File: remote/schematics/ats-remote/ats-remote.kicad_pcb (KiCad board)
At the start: 4 copper layers, 34 x 39 mm, 34 parts, among them J1 PWR, J4 Conn_01x02_Male, U1 RFM95W-915S2

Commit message: update schematic and pcb
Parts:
- removed GPS ANT: GPS_ANT, ats-remote:GPS_ANT_SR4G008
- added AE1: GPS_ANT, ats-remote:GPS_ANT_SR4G008, F.Cu at (140.5, 38.3)
- added C14: 10n, Capacitor_SMD:C_0805_2012Metric_Pad1.18x1.45mm_HandSolder, F.Cu at (140.2, 43.6)
- added L3: 33n, Inductor_SMD:L_0603_1608Metric_Pad1.05x0.95mm_HandSolder, F.Cu at (142.1, 46.9)
- added L4: 33n, Inductor_SMD:L_0603_1608Metric_Pad1.05x0.95mm_HandSolder, F.Cu at (142.1, 43.4)
- AE2: renamed from LORA ANT
- C13, C8: value 2.2u -> 2u2
- C6: value 100p -> 2u2
- C7: value 100p -> 10n
- J3: renamed from SPI; value Conn_01x04_Male -> SPI
- J4: value Conn_01x02_Male -> UART
- R1, R2: value 2.2k -> 2k2
- R5: value 22 -> 2k2
- moved J3 3.90 mm to (114.2, 62.9), turned to 180 degrees
- moved L1 3.06 mm to (140.0, 47.3)
- moved C11 2.77 mm to (142.4, 51.1), turned to 90 degrees
- moved D1 1.20 mm to (141.3, 65.3)
- moved D2 1.20 mm to (141.3, 68.0)
- moved D3 1.20 mm to (141.3, 62.5)
- moved C8 1.00 mm to (140.2, 51.1), turned to 90 degrees
- renumbered ICSP to J2, PIC18 to U2, YIC to U3
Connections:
- J3 pad 1: LORA_SCK -> LORA_NSS
- J3 pad 2: LORA_MOSI -> LORA_MISO
- J3 pad 3: LORA_MISO -> LORA_MOSI
- J3 pad 4: LORA_NSS -> LORA_SCK
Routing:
- net +3V3: track 32.1 -> 109.8 mm
- net Net-(AE1-Pad2): track 0.00 -> 4.19 mm
- net GND: track 69.2 -> 71.3 mm, vias 59 -> 83
- net Net-(C11-Pad2): track 15.4 -> 13.4 mm
- net Net-(D2-Pad2): track 3.76 -> 2.56 mm
- net Net-(D1-Pad2): track 3.76 -> 2.56 mm
- net Net-(D3-Pad2): track 3.76 -> 2.56 mm
- net LORA_NSS: track 45.5 -> 46.5 mm
- net Net-(C14-Pad2): track 10.1 -> 9.14 mm
- added copper zone on 3v3.Cu, net GND
- removed copper zone on 3v3.Cu, net +3V3
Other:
- net class 50ohm @ JLCPCB type JLC7628 added: clearance 0.6, trace_width 0.29337, via_dia 0.5, via_drill 0.3
- rule trace_min: 0.3 -> 0.2

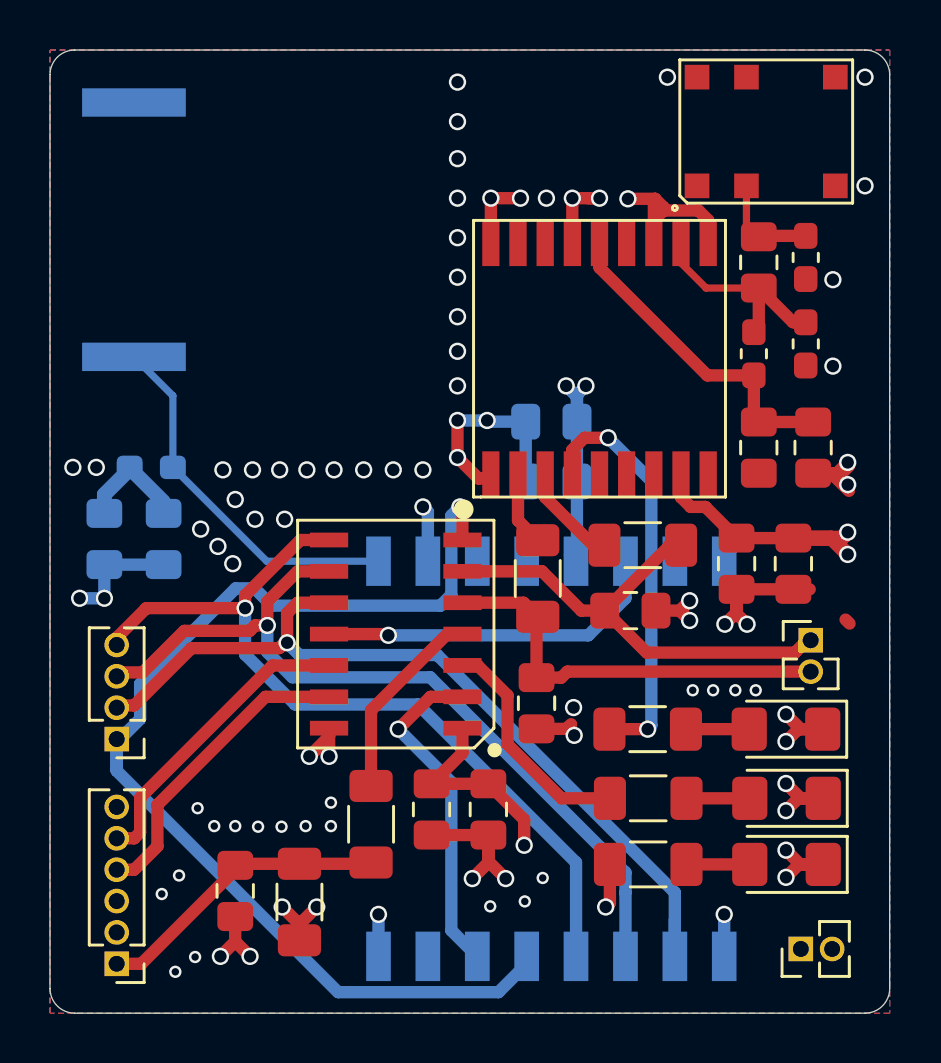
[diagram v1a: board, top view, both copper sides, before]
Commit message: add silk screen
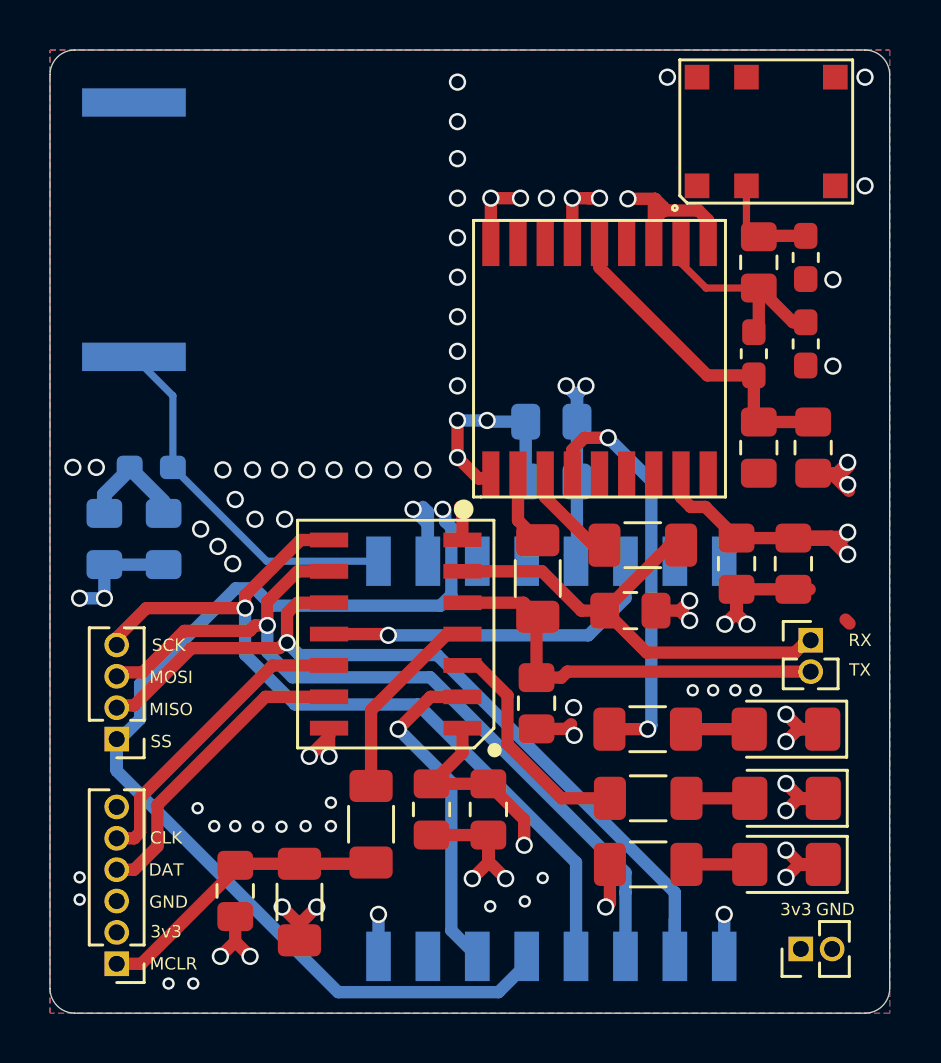
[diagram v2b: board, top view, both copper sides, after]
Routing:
- net GND: track 71.3 -> 73.7 mm
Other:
- board text added: "3v3"
- board text added: "CLK"
- board text added: "DAT"
- board text added: "GND"
- board text added: "MCLR"
- board text added: "MISO"
- board text added: "MOSI"
- board text added: "RX"
- board text added: "SCK"
- board text added: "SS"
- board text added: "TX"
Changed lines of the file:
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@@
   (general
     (thickness 1.6)
-    (drawings 8)
-    (tracks 395)
+    (drawings 21)
+    (tracks 398)
     (zones 0)
     (modules 37)
@@
   )
   (layers
-    (0 F.Cu signal)
-    (1 GND.Cu power)
-    (2 3v3.Cu power)
+    (0 F.Cu signal hide)
+    (1 GND.Cu power hide)
+    (2 3v3.Cu power hide)
     (31 B.Cu signal)
     (32 B.Adhes user)
@@
     (pad 2 smd rect (at -6.425 4.6 270) (size 1.15 4.2) (layers B.Cu B.Paste B.Mask))
   )
+  (gr_text TX (at 144.3 60.1) (layer F.SilkS)
+    (effects (font (size 0.5 0.5) (thickness 0.1)))
+  )
+  (gr_text "RX\n" (at 144.3 58.9) (layer F.SilkS)
+    (effects (font (size 0.5 0.5) (thickness 0.1)))
+  )
+  (gr_text "GND\n" (at 143.3 69.8) (layer F.SilkS)
+    (effects (font (size 0.5 0.5) (thickness 0.1)))
+  )
+  (gr_text "3v3\n" (at 141.7 69.8) (layer F.SilkS)
+    (effects (font (size 0.5 0.5) (thickness 0.1)))
+  )
+  (gr_text CLK (at 116.2 66.9) (layer F.SilkS)
+    (effects (font (size 0.5 0.5) (thickness 0.1)))
+  )
+  (gr_text DAT (at 116.2 68.2) (layer F.SilkS)
+    (effects (font (size 0.5 0.5) (thickness 0.1)))
+  )
+  (gr_text "GND\n" (at 116.3 69.5) (layer F.SilkS)
+    (effects (font (size 0.5 0.5) (thickness 0.1)))
+  )
+  (gr_text "3v3\n" (at 116.2 70.7) (layer F.SilkS)
+    (effects (font (size 0.5 0.5) (thickness 0.1)))
+  )
+  (gr_text MCLR (at 116.5 72) (layer F.SilkS)
+    (effects (font (size 0.5 0.5) (thickness 0.1)))
+  )
+  (gr_text "SCK\n" (at 116.3 59.1) (layer F.SilkS)
+    (effects (font (size 0.5 0.5) (thickness 0.1)))
+  )
+  (gr_text MOSI (at 116.4 60.4) (layer F.SilkS)
+    (effects (font (size 0.5 0.5) (thickness 0.1)))
+  )
+  (gr_text "MISO\n" (at 116.4 61.7) (layer F.SilkS)
+    (effects (font (size 0.5 0.5) (thickness 0.1)))
+  )
+  (gr_text SS (at 116 63) (layer F.SilkS)
+    (effects (font (size 0.5 0.5) (thickness 0.1)))
+  )
   (gr_arc (start 112.5 73) (end 111.5 73) (angle -90) (layer Edge.Cuts) (width 0.05))
   (gr_arc (start 144.5 73) (end 144.5 74) (angle -90) (layer Edge.Cuts) (width 0.05))
@@
   (segment (start 127.750001 64.650001) (end 127.750001 70.650001) (width 0.5) (layer B.Cu) (net 1))
   (segment (start 125.6 62.5) (end 127.750001 64.650001) (width 0.5) (layer B.Cu) (net 1))
-  (via (at 128.1 53.5) (size 0.7) (drill 0.5) (layers F.Cu B.Cu) (net 2))
+  (via (at 127.4 53.6) (size 0.7) (drill 0.5) (layers F.Cu B.Cu) (net 2))
   (segment (start 130.8 71.389998) (end 130.8 71.389998) (width 0.5) (layer B.Cu) (net 2))
   (segment (start 119.015999 56.799999) (end 115.150001 60.665997) (width 0.5) (layer B.Cu) (net 2))
@@
   (segment (start 127.310003 57.499999) (end 120.484001 57.499999) (width 0.5) (layer B.Cu) (net 2))
   (segment (start 127.750001 57.060001) (end 127.310003 57.499999) (width 0.5) (layer B.Cu) (net 2))
-  (segment (start 127.750001 53.849999) (end 127.750001 57.060001) (width 0.5) (layer B.Cu) (net 2))
-  (segment (start 128.1 53.5) (end 127.750001 53.849999) (width 0.5) (layer B.Cu) (net 2))
   (segment (start 114.2 64.184002) (end 114.2 62.81) (width 0.5) (layer B.Cu) (net 2))
   (segment (start 123.165999 73.150001) (end 114.2 64.184002) (width 0.5) (layer B.Cu) (net 2))
@@
   (segment (start 115.150001 62.086001) (end 114.336002 62.9) (width 0.5) (layer B.Cu) (net 2))
   (segment (start 115.150001 60.665997) (end 115.150001 62.086001) (width 0.5) (layer B.Cu) (net 2))
+  (segment (start 127.50001 54.090008) (end 127.50001 53.6) (width 0.5) (layer B.Cu) (net 2))
+  (segment (start 127.750001 54.339999) (end 127.50001 54.090008) (width 0.5) (layer B.Cu) (net 2))
+  (segment (start 127.750001 57.060001) (end 127.750001 54.339999) (width 0.5) (layer B.Cu) (net 2))
   (via (at 119.4 57.6) (size 0.7) (drill 0.5) (layers F.Cu B.Cu) (net 3))
   (segment (start 132.8 72.010002) (end 132.8 72.010002) (width 0.5) (layer B.Cu) (net 3))
@@
   (via (at 125.4 52) (size 0.7) (drill 0.5) (layers F.Cu B.Cu) (net 18))
   (via (at 126.6 52) (size 0.7) (drill 0.5) (layers F.Cu B.Cu) (net 18))
-  (via (at 126.6 53.5) (size 0.7) (drill 0.5) (layers F.Cu B.Cu) (net 18))
+  (via (at 126.2 53.6) (size 0.7) (drill 0.5) (layers F.Cu B.Cu) (net 18))
   (segment (start 126.8 53.7) (end 126.6 53.5) (width 0.5) (layer B.Cu) (net 18))
   (segment (start 126.8 55.7) (end 126.8 53.7) (width 0.5) (layer B.Cu) (net 18))
@@
   (via (at 129.325 69.675) (size 0.5) (drill 0.3) (layers F.Cu B.Cu) (net 18))
   (via (at 131.45 68.525) (size 0.5) (drill 0.3) (layers F.Cu B.Cu) (net 18))
-  (via (at 117.375 71.725) (size 0.5) (drill 0.3) (layers F.Cu B.Cu) (net 18))
-  (via (at 116.575 72.325) (size 0.5) (drill 0.3) (layers F.Cu B.Cu) (net 18))
-  (via (at 116.725 68.425) (size 0.5) (drill 0.3) (layers F.Cu B.Cu) (net 18))
-  (via (at 116.025 69.175) (size 0.5) (drill 0.3) (layers F.Cu B.Cu) (net 18))
+  (via (at 117.3 72.8) (size 0.5) (drill 0.3) (layers F.Cu B.Cu) (net 18))
+  (via (at 116.3 72.8) (size 0.5) (drill 0.3) (layers F.Cu B.Cu) (net 18))
+  (via (at 112.7 68.5) (size 0.5) (drill 0.3) (layers F.Cu B.Cu) (net 18))
+  (via (at 112.7 69.4) (size 0.5) (drill 0.3) (layers F.Cu B.Cu) (net 18))
   (via (at 117.475 65.7) (size 0.5) (drill 0.3) (layers F.Cu B.Cu) (net 18))
   (via (at 118.15 66.425) (size 0.5) (drill 0.3) (layers F.Cu B.Cu) (net 18))
@@
   (segment (start 143.3375 52.1375) (end 143.8 52.6) (width 0.5) (layer F.Cu) (net 18))
   (segment (start 142.4 52.1375) (end 143.3375 52.1375) (width 0.5) (layer F.Cu) (net 18))
+  (segment (start 126.8 54.2) (end 126.2 53.6) (width 0.5) (layer B.Cu) (net 18))
+  (segment (start 126.8 55.7) (end 126.8 54.2) (width 0.5) (layer B.Cu) (net 18))
   (segment (start 121.64 67.91) (end 121.6 67.95) (width 0.5) (layer F.Cu) (net 19))
   (segment (start 119.0625 67.95) (end 119 68.0125) (width 0.5) (layer F.Cu) (net 19))

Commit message: update silk screen
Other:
- board text added: "GPS ANT"
- board text added: "LORA ANT"
- board text added: "PIC18F06"
- board text added: "YIC71009EBGG"
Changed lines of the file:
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@@
   (general
     (thickness 1.6)
-    (drawings 21)
+    (drawings 25)
     (tracks 398)
     (zones 0)
@@
   )
   (layers
-    (0 F.Cu signal hide)
-    (1 GND.Cu power hide)
-    (2 3v3.Cu power hide)
+    (0 F.Cu signal)
+    (1 GND.Cu power)
+    (2 3v3.Cu power)
     (31 B.Cu signal)
     (32 B.Adhes user)
@@
     (pad 2 smd rect (at -6.425 4.6 270) (size 1.15 4.2) (layers B.Cu B.Paste B.Mask))
   )
+  (gr_text "GPS ANT" (at 136.5 39.5 90) (layer F.SilkS)
+    (effects (font (size 0.5 0.5) (thickness 0.1)))
+  )
+  (gr_text "LORA ANT\n" (at 115.2 48.8) (layer B.SilkS)
+    (effects (font (size 0.5 0.5) (thickness 0.1)) (justify mirror))
+  )
+  (gr_text YIC71009EBGG (at 136.2 53.6) (layer F.SilkS)
+    (effects (font (size 0.5 0.5) (thickness 0.1)))
+  )
+  (gr_text PIC18F06 (at 123.2 53.5) (layer F.SilkS)
+    (effects (font (size 0.5 0.5) (thickness 0.1)))
+  )
   (gr_text TX (at 144.3 60.1) (layer F.SilkS)

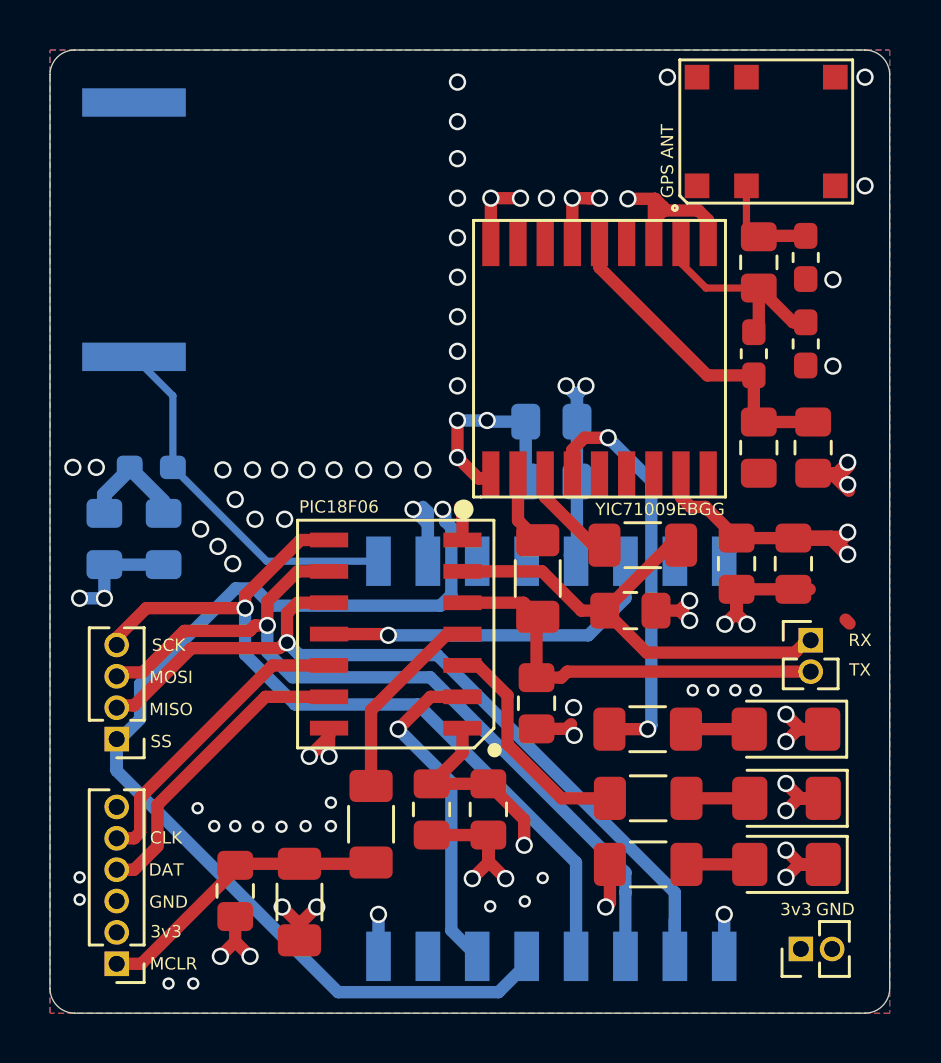
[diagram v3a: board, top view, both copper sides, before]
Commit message: fix lora nss via and gps ant grounds
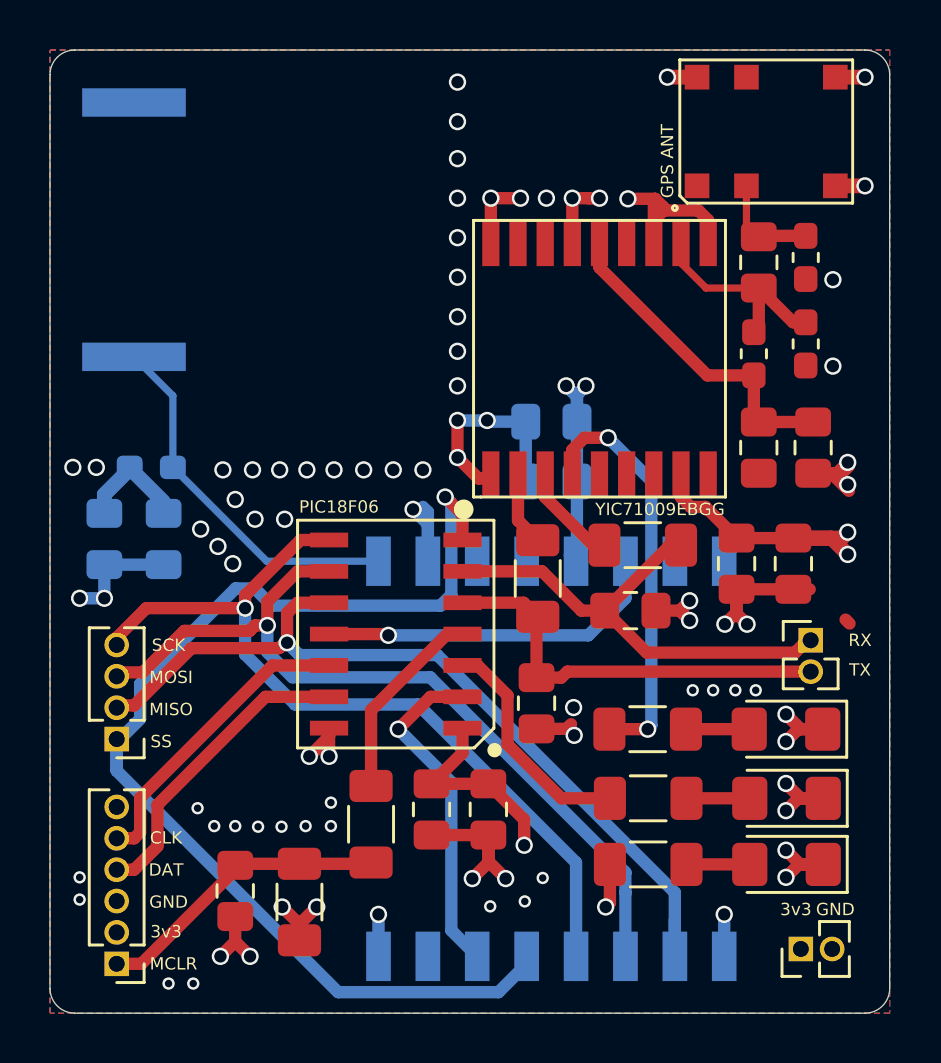
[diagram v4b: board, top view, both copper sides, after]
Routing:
- net GND: track 73.7 -> 77.3 mm
- net LORA_NSS: track 46.4 -> 47.5 mm
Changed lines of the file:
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@@
     (thickness 1.6)
     (drawings 25)
-    (tracks 398)
+    (tracks 400)
     (zones 0)
     (modules 37)
@@
   )
   (setup
-    (last_trace_width 0.5)
+    (last_trace_width 0.6)
     (user_trace_width 0.29337)
     (user_trace_width 0.3)
@@
   (segment (start 127.750001 64.650001) (end 127.750001 70.650001) (width 0.5) (layer B.Cu) (net 1))
   (segment (start 125.6 62.5) (end 127.750001 64.650001) (width 0.5) (layer B.Cu) (net 1))
-  (via (at 127.4 53.6) (size 0.7) (drill 0.5) (layers F.Cu B.Cu) (net 2))
+  (via (at 127.5 53.1) (size 0.7) (drill 0.5) (layers F.Cu B.Cu) (net 2))
   (segment (start 130.8 71.389998) (end 130.8 71.389998) (width 0.5) (layer B.Cu) (net 2))
-  (segment (start 119.015999 56.799999) (end 115.150001 60.665997) (width 0.5) (layer B.Cu) (net 2))
-  (segment (start 119.784001 56.799999) (end 119.015999 56.799999) (width 0.5) (layer B.Cu) (net 2))
-  (segment (start 120.484001 57.499999) (end 119.784001 56.799999) (width 0.5) (layer B.Cu) (net 2))
-  (segment (start 127.310003 57.499999) (end 120.484001 57.499999) (width 0.5) (layer B.Cu) (net 2))
-  (segment (start 127.750001 57.060001) (end 127.310003 57.499999) (width 0.5) (layer B.Cu) (net 2))
   (segment (start 114.2 64.184002) (end 114.2 62.81) (width 0.5) (layer B.Cu) (net 2))
   (segment (start 123.165999 73.150001) (end 114.2 64.184002) (width 0.5) (layer B.Cu) (net 2))
@@
   (segment (start 130.8 72.010002) (end 129.660001 73.150001) (width 0.5) (layer B.Cu) (net 2))
   (segment (start 130.8 71.7) (end 130.8 72.010002) (width 0.5) (layer B.Cu) (net 2))
-  (segment (start 128.2 53.6) (end 128.1 53.5) (width 0.5) (layer F.Cu) (net 2))
-  (segment (start 128.2 54.84) (end 128.2 53.6) (width 0.5) (layer F.Cu) (net 2))
   (segment (start 130.8 71.389998) (end 130.8 71.7) (width 0.5) (layer B.Cu) (net 2))
   (segment (start 114.2 64.184002) (end 114.2 62.9) (width 0.5) (layer B.Cu) (net 2))
-  (segment (start 114.336002 62.9) (end 114.2 62.9) (width 0.5) (layer B.Cu) (net 2))
-  (segment (start 115.150001 62.086001) (end 114.336002 62.9) (width 0.5) (layer B.Cu) (net 2))
-  (segment (start 115.150001 60.665997) (end 115.150001 62.086001) (width 0.5) (layer B.Cu) (net 2))
-  (segment (start 127.50001 54.090008) (end 127.50001 53.6) (width 0.5) (layer B.Cu) (net 2))
-  (segment (start 127.750001 54.339999) (end 127.50001 54.090008) (width 0.5) (layer B.Cu) (net 2))
-  (segment (start 127.750001 57.060001) (end 127.750001 54.339999) (width 0.5) (layer B.Cu) (net 2))
+  (segment (start 127.750001 57.060001) (end 127.750001 53.350001) (width 0.5) (layer B.Cu) (net 2))
+  (segment (start 120.484001 57.499999) (end 127.310003 57.499999) (width 0.5) (layer B.Cu) (net 2))
+  (segment (start 127.310003 57.499999) (end 127.750001 57.060001) (width 0.5) (layer B.Cu) (net 2))
+  (segment (start 119.784001 56.799999) (end 120.484001 57.499999) (width 0.5) (layer B.Cu) (net 2))
+  (segment (start 127.750001 53.350001) (end 127.5 53.1) (width 0.5) (layer B.Cu) (net 2))
+  (segment (start 119.015999 56.799999) (end 119.784001 56.799999) (width 0.5) (layer B.Cu) (net 2))
+  (segment (start 115.150001 60.665997) (end 119.015999 56.799999) (width 0.5) (layer B.Cu) (net 2))
+  (segment (start 115.150001 62.086001) (end 115.150001 60.665997) (width 0.5) (layer B.Cu) (net 2))
+  (segment (start 114.336002 62.9) (end 115.150001 62.086001) (width 0.5) (layer B.Cu) (net 2))
+  (segment (start 114.2 62.9) (end 114.336002 62.9) (width 0.5) (layer B.Cu) (net 2))
+  (segment (start 128.2 53.8) (end 127.5 53.1) (width 0.5) (layer F.Cu) (net 2))
+  (segment (start 128.2 54.84) (end 128.2 53.8) (width 0.5) (layer F.Cu) (net 2))
   (via (at 119.4 57.6) (size 0.7) (drill 0.5) (layers F.Cu B.Cu) (net 3))
   (segment (start 132.8 72.010002) (end 132.8 72.010002) (width 0.5) (layer B.Cu) (net 3))
@@
   (segment (start 126.8 54.2) (end 126.2 53.6) (width 0.5) (layer B.Cu) (net 18))
   (segment (start 126.8 55.7) (end 126.8 54.2) (width 0.5) (layer B.Cu) (net 18))
+  (segment (start 143.3 36.1) (end 144.5 36.1) (width 0.6) (layer F.Cu) (net 18))
+  (segment (start 137.7 36.1) (end 136.5 36.1) (width 0.6) (layer F.Cu) (net 18))
+  (segment (start 143.3 40.5) (end 144.5 40.5) (width 0.6) (layer F.Cu) (net 18))
   (segment (start 121.64 67.91) (end 121.6 67.95) (width 0.5) (layer F.Cu) (net 19))
   (segment (start 119.0625 67.95) (end 119 68.0125) (width 0.5) (layer F.Cu) (net 19))
